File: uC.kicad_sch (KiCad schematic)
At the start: 10 parts, among them J3 Conn_01x04, U3 STM32G431KBT6

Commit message: added xtal
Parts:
- added C10: 100nF, symbol Device:C
- added Y1: ECS-2520MV-xxx-xx, Oscillator:Oscillator_SMD_ECS_2520MV-xxx-xx-4Pin_2.5x2.0mm, symbol Oscillator:ECS-2520MV-xxx-xx
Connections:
- net +3.3V: now also C10.1, Y1.1 (Tri-State), Y1.4 (VDD)
- net GNDD: now also U3.3 (PF1-OSC_OUT), C10.2, Y1.2 (GND)
- net at U3.2 (PF0-OSC_IN): now also Y1.3 (OUT)
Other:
- note added: "Vicor 42550 connector"

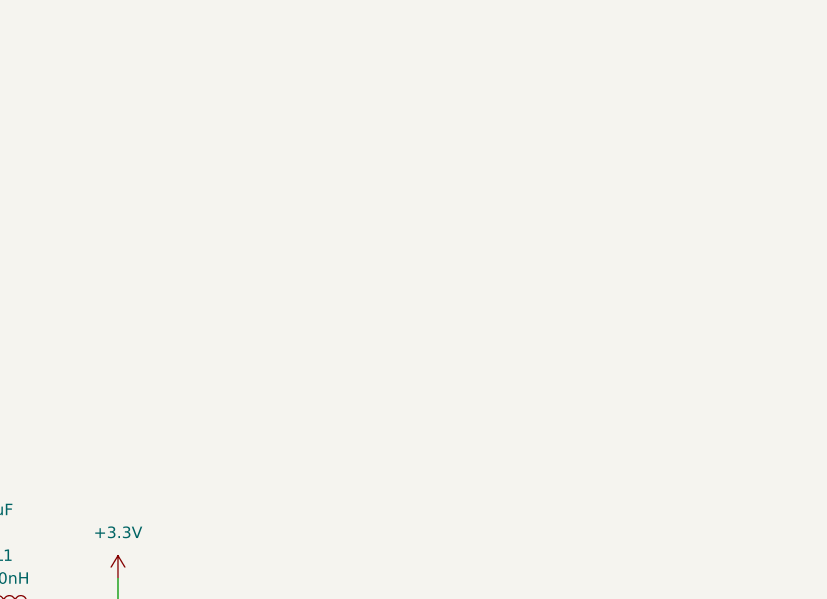
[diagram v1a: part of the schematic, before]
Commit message: found the correct i2c logic level shifter.
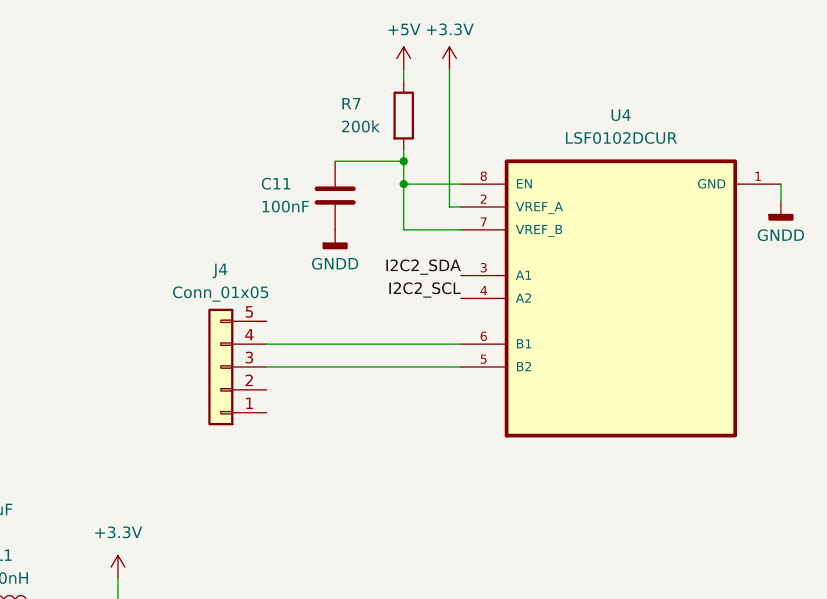
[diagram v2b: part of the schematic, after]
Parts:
- added C11: 100nF, symbol Device:C
- added J4: Conn_01x05, symbol Connector_Generic:Conn_01x05
- added R7: 200k, symbol Device:R
- added U4: LSF0102DCUR, LSF0102DCUR:SOP50P310X90-8N, symbol LSF0102DCUR:LSF0102DCUR
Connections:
- net +3.3V: now also U4.2 (VREF_A)
- net GNDD: now also C11.2, U4.1 (GND)
- net I2C2_SCL: now also U4.4 (A2)
- net I2C2_SDA: now also U4.3 (A1)
- new net: C11.1, R7.2, U4.7 (VREF_B), U4.8 (EN)
- new net: J4.3 (Pin_3), U4.5 (B2)
- new net: J4.4 (Pin_4), U4.6 (B1)
- new net +5V: R7.1

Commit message: made todo, added power
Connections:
- net +5V: now also J4.5 (Pin_5)
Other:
- note added: "--> Vicor 42550"
- note removed: "Vicor 42550 connector"
- moved on the sheet: C11, J4, R7, U4

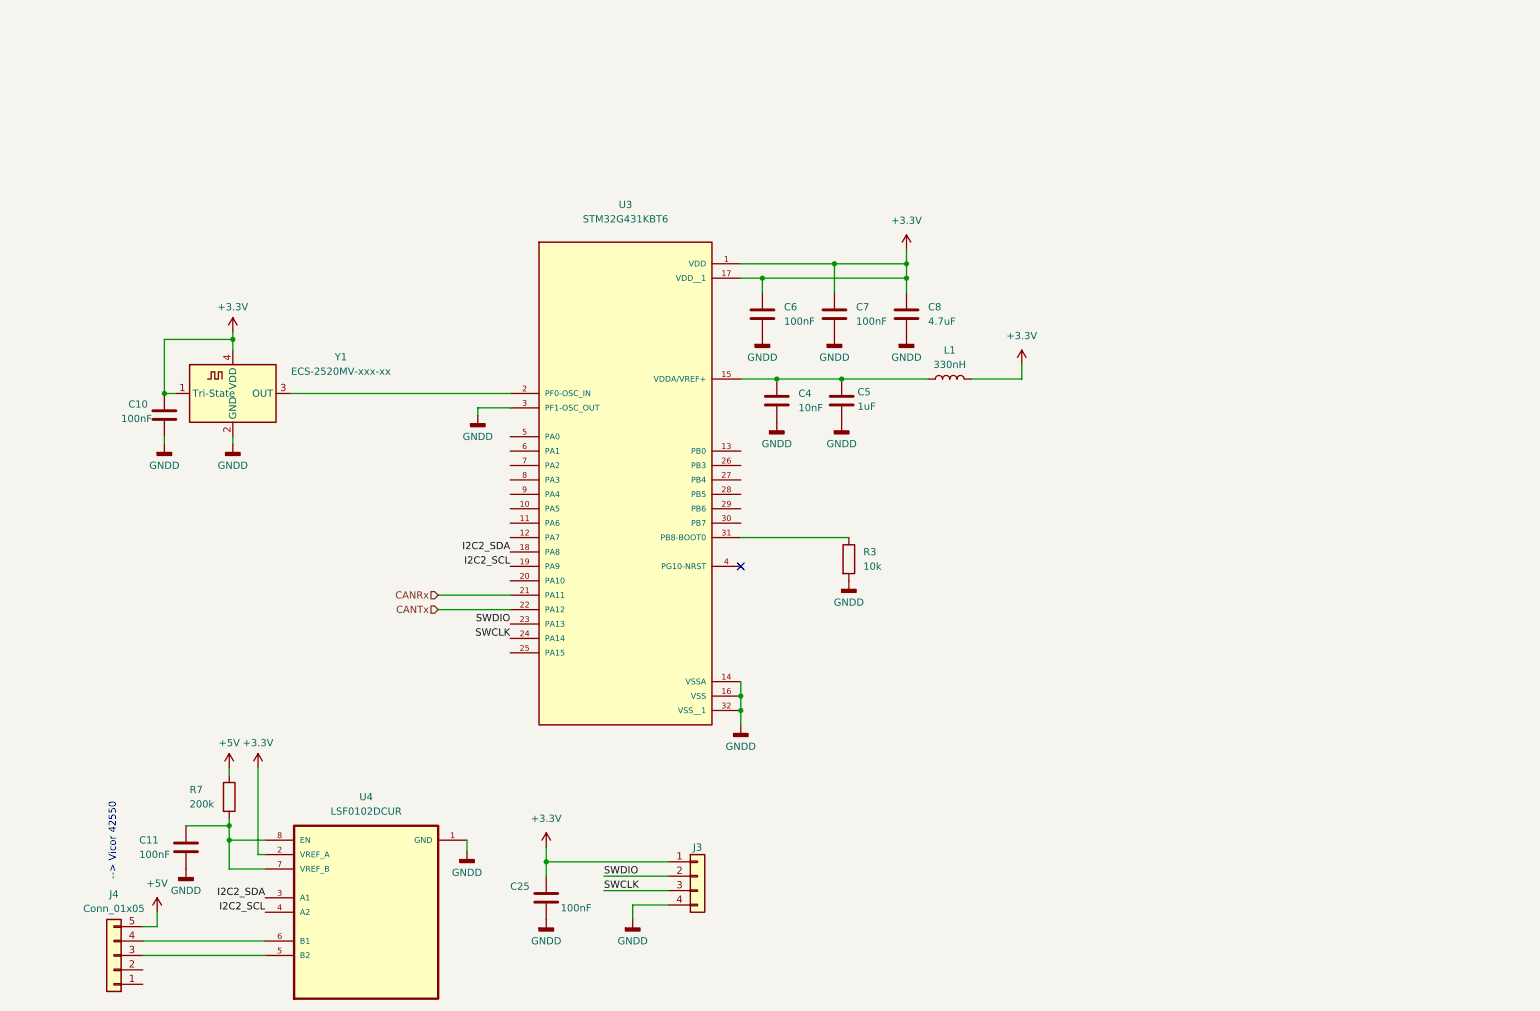
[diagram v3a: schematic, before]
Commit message: fixed bcm connector, added thermistors something else too prolly
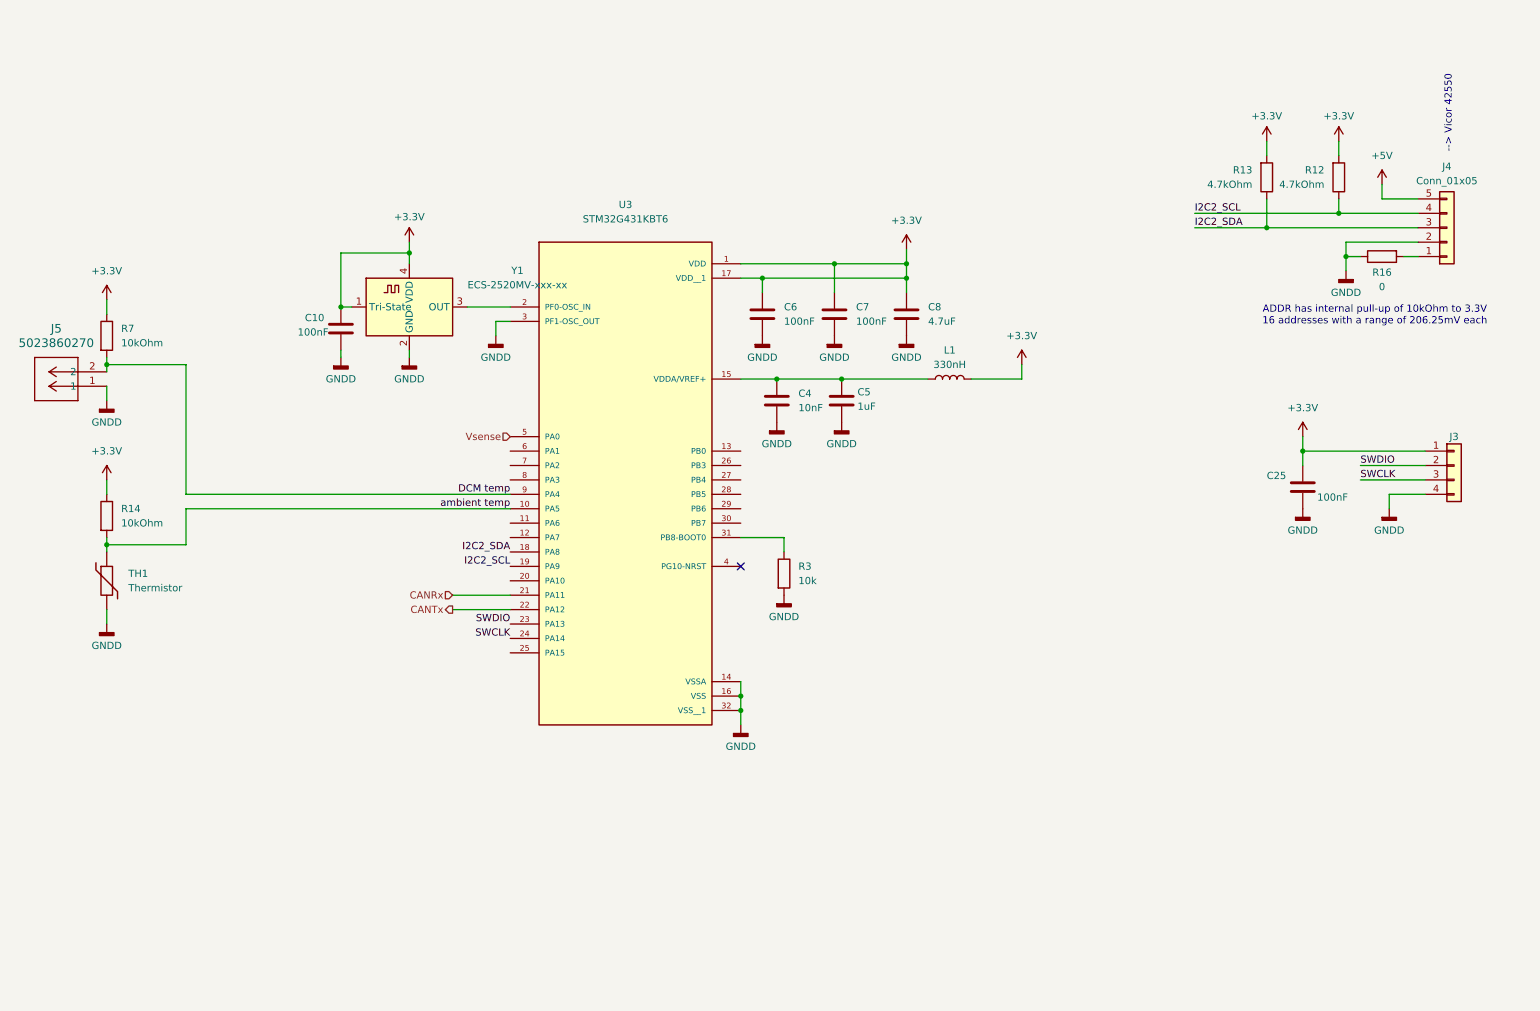
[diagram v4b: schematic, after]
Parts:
- removed C11: 100nF, symbol Device:C
- removed U4: LSF0102DCUR, LSF0102DCUR:SOP50P310X90-8N, symbol LSF0102DCUR:LSF0102DCUR
- added J5: 5023860270, CONN_502386-02xx_MOL, symbol 2026-03-29_17-20-59:5023860270
- added R12, R13: 4.7kOhm, symbol Device:R
- added R14: 10kOhm, symbol Device:R
- added R16: 0, symbol Device:R
- added TH1: Thermistor, symbol Device:Thermistor
- R7: value 200k -> 10kOhm
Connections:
- net +3.3V: now also R7.1, R12.2, R13.2, R14.1
- net +5V: no longer R7.1
- net GNDD: now also J4.2 (Pin_2), J5.1, R16.1, TH1.2
- net I2C2_SCL: now also J4.4 (Pin_4), R12.1
- net I2C2_SDA: now also J4.3 (Pin_3), R13.1
- net DCM temp: now reaches R7.2
- net DCM temp: now also U3.9 (PA4), J5.2
- net ambient temp: now reaches U3.10 (PA5)
- net ambient temp: now also R14.2, TH1.1
- net Vsense: now reaches U3.5 (PA0)
- net at J4.1 (Pin_1): now also R16.2
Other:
- note added: "ADDR has internal pull-up of 10kOhm to 3.3V 16 addresses with a range of 206.25mV each"
- moved on the sheet: C10, C25, J3, J4, R3, Y1
